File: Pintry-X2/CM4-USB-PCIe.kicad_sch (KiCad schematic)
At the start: 19 parts

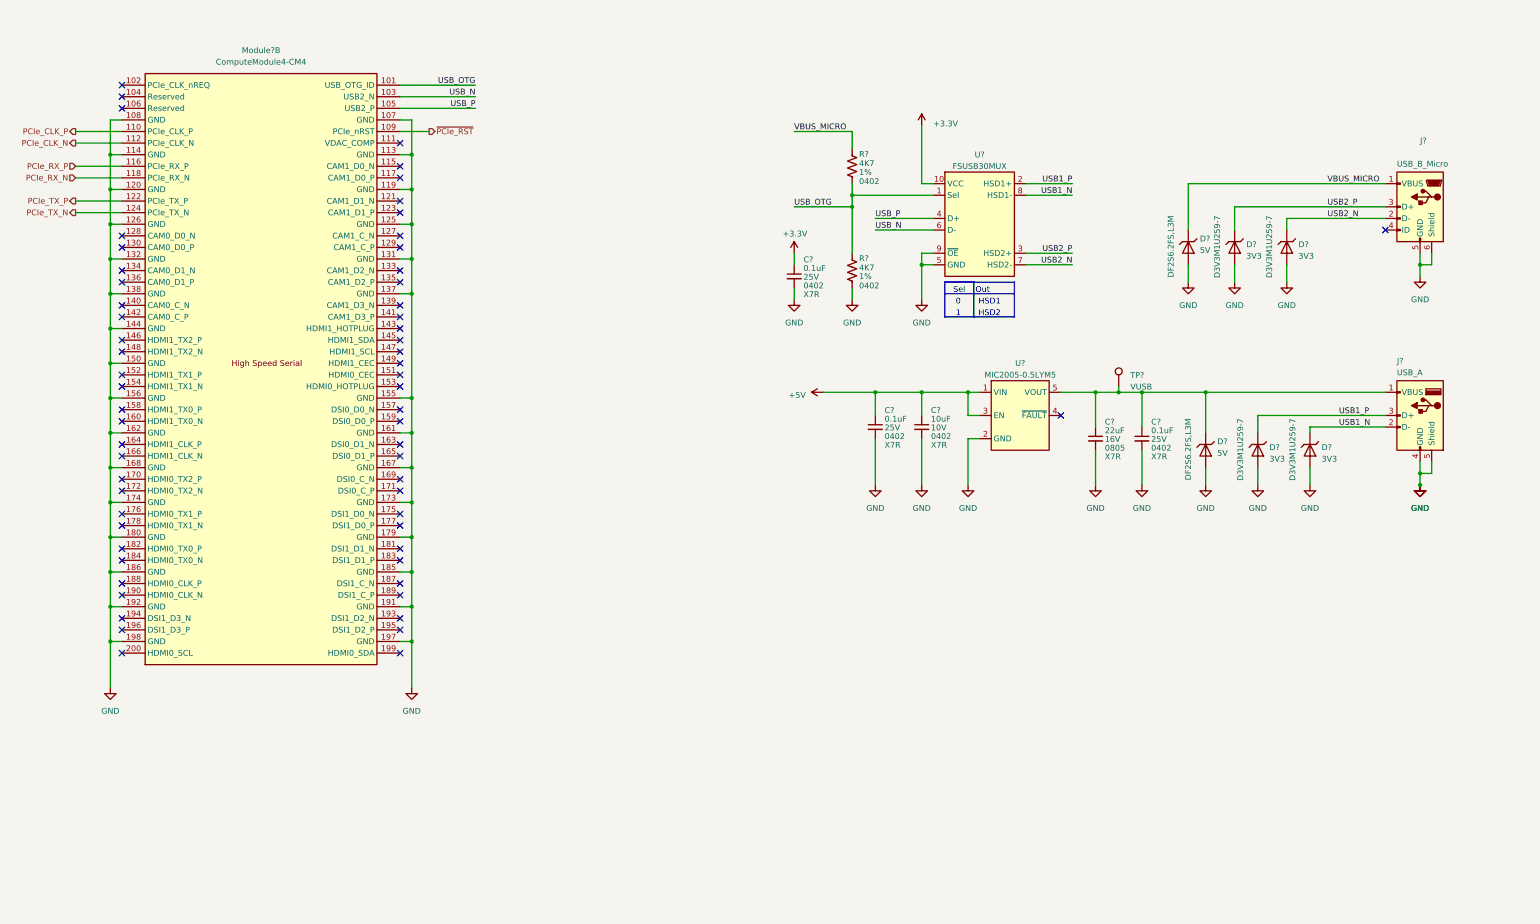
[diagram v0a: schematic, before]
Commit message: Cleaned up schematic
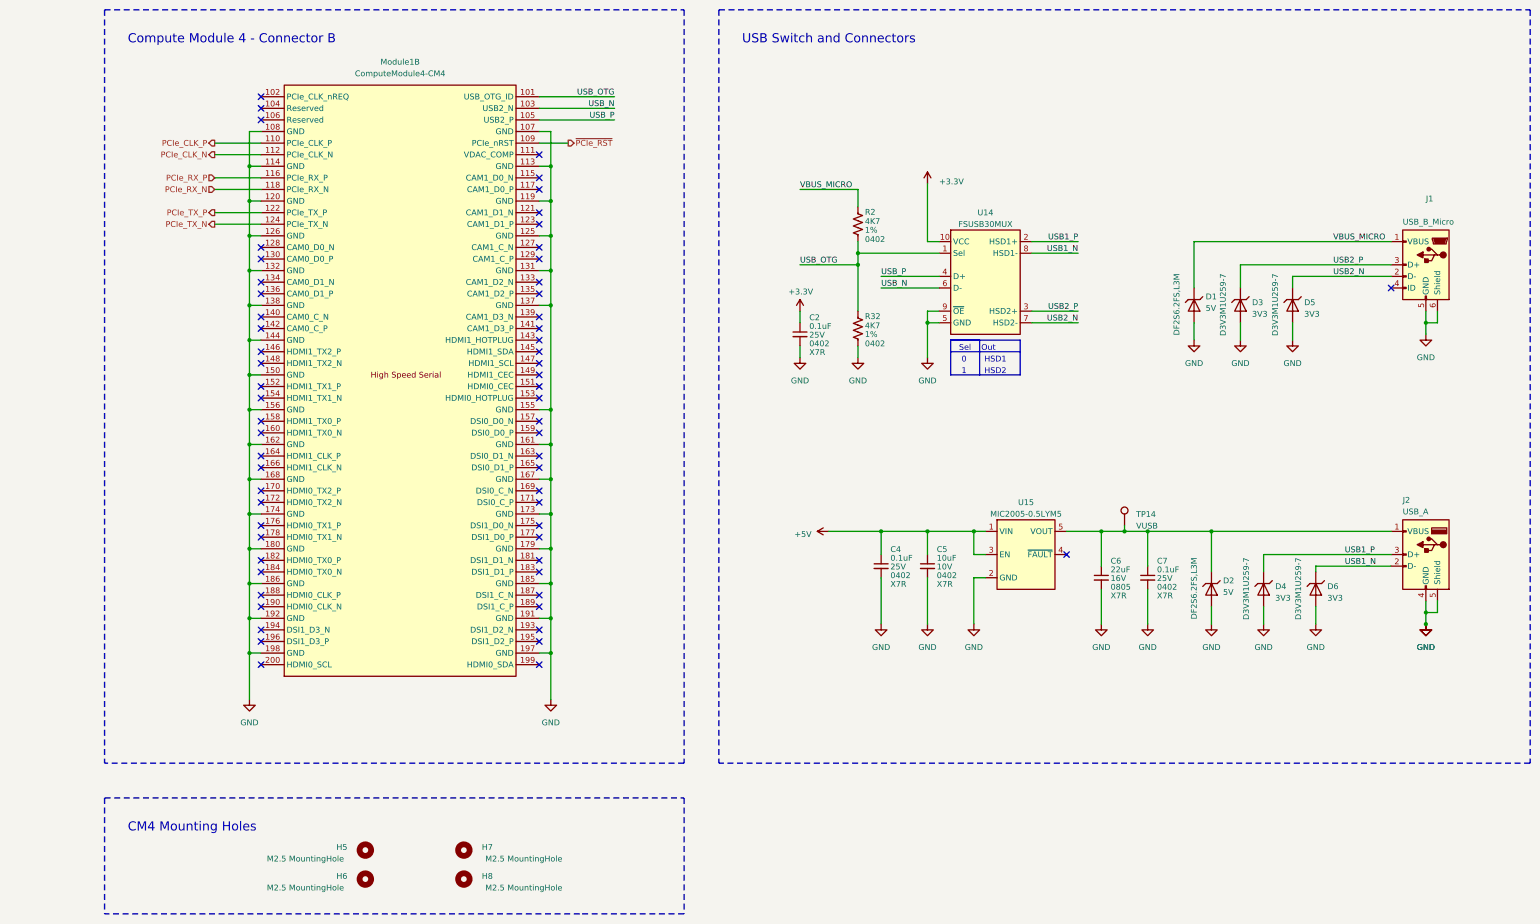
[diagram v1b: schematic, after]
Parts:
- added H5, H6, H7, H8: M2.5 MountingHole, MountingHole:MountingHole_2.7mm_M2.5, symbol Mechanical:MountingHole
- gave numbers to parts that had none: 19
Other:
- note added: "CM4 Mounting Holes"
- note added: "Compute Module 4 - Connector B"
- note added: "USB Switch and Connectors"
- moved on the sheet: C2, C4, C5, C6, C7, D1, D2, D3, D4, D5, D6, J1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

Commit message: Finished Shematic. Starting PCB
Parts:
- removed H5, H6, H7, H8: M2.5 MountingHole, MountingHole:MountingHole_2.7mm_M2.5, symbol Mechanical:MountingHole
- J1: footprint Connector_USB:USB_Micro-B_Amphenol_10103594-0001LF_Horizontal -> PintryParts-Footprints:USB_Micro-B_Amphenol_10103594-0001LF_Horizontal
- J2: footprint Connector_USB:USB_A_Wuerth_614004134726_Horizontal -> PintryParts-Footprints:USB_A_Amphenol_ICC_73725-11A0BLF_Horizontal
- Module1: footprint CM4IO:Raspberry-Pi-4-Compute-Module -> PintryParts-Footprints:Raspberry-Pi-4-Compute-Module
- TP14: footprint TestPoint:TestPoint_Pad_D2.5mm -> TestPoint:TestPoint_Pad_D1.0mm
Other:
- note removed: "CM4 Mounting Holes"

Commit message: PCB Routing Complete - needs review
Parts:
- added Q3: BSS138PW, Package_TO_SOT_SMD:SOT-323_SC-70, symbol PintryParts-Symbols:BSS138PW
- added R16: 4K7, PintryParts-Footprints:R_0402_1005Metric, symbol Device:R_US
- TP14: footprint TestPoint:TestPoint_Pad_D1.0mm -> PintryParts-Footprints:TestPoint_Pad_D1.0mm
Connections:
- net GND: now also Q3.2 (S)
- net VBUS_MICRO: now also R16.2
- net ~PCIe_RST renamed ~{PCIe_RST}
- new net: Q3.1 (G), R16.1
- new net ~{RPIBOOT}: Q3.3 (D)
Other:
- moved on the sheet: D1, D3, D5, J1

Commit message: Final touches and generate Gerbers to be sent to fab
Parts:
- added R35: 100k, PintryParts-Footprints:R_0402_1005Metric, symbol Device:R_US
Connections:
- net GND: now also R35.2
- net at Q3.1 (G), R16.1: now also R35.1
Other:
- moved on the sheet: D1, D3, D5, R16

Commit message: Fixed ON/OFF Button
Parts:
- R16: fit_field dnf -> (none)
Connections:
- net +5V: no longer U15.3 (EN)
- net GND: now also U15.3 (EN)
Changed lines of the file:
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@@
   (junction (at 236.22 121.92) (diameter 0.9144) (color 0 0 0 0))
   (junction (at 236.22 167.64) (diameter 0.9144) (color 0 0 0 0))
-  (junction (at 246.38 167.64) (diameter 0.9144) (color 0 0 0 0))
+  (junction (at 246.38 177.8) (diameter 0) (color 0 0 0 0))
   (junction (at 274.32 167.64) (diameter 0.9144) (color 0 0 0 0))
   (junction (at 279.4 167.64) (diameter 0.9144) (color 0 0 0 0))
@@
     (stroke (width 0) (type solid) (color 0 0 0 0))
   )
+  (wire (pts (xy 236.22 167.64) (xy 248.92 167.64))
+    (stroke (width 0) (type solid) (color 0 0 0 0))
+  )
   (wire (pts (xy 236.22 177.8) (xy 236.22 187.96))
     (stroke (width 0) (type solid) (color 0 0 0 0))
@@
     (stroke (width 0) (type solid) (color 0 0 0 0))
   )
-  (wire (pts (xy 246.38 167.64) (xy 236.22 167.64))
-    (stroke (width 0) (type solid) (color 0 0 0 0))
-  )
-  (wire (pts (xy 246.38 172.72) (xy 246.38 167.64))
-    (stroke (width 0) (type solid) (color 0 0 0 0))
+  (wire (pts (xy 246.38 172.72) (xy 246.38 177.8))
+    (stroke (width 0) (type default) (color 0 0 0 0))
   )
   (wire (pts (xy 246.38 177.8) (xy 246.38 187.96))
-    (stroke (width 0) (type solid) (color 0 0 0 0))
-  )
-  (wire (pts (xy 248.92 167.64) (xy 246.38 167.64))
     (stroke (width 0) (type solid) (color 0 0 0 0))
   )
@@
       (effects (font (size 1.27 1.27)) (justify right))
     )
-    (property "fit_field" "dnf" (id 6) (at 295.91 104.14 0)
-      (effects (font (size 1.27 1.27)) hide)
-    )
-    (pin "1")
+    (pin "1")
